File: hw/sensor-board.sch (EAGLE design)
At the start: 17 parts, among them U1 LT1762EMS8-3.3PBF, U2 ULN2003LVPWR, U3 ULN2003LVPWR, U4 PCA9685PW, U5 AT42QT1110-AU, X1 MOLEX-501331-1007, X2 MOLEX-501953-0407, X3 MOLEX-501953-0407, X4 MOLEX-501953-0407

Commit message: Connect capsense controller/buttons/B2B connector.
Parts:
- added C10, C11, C12, C5, C6, C7, C8, C9: 0.015uF 16V, rcl:C-EUC0402K
- added R1, R2, R3, R4, R5, R6, R7, R8: 4.7k, myrcl:R-EU_NKR0402
- added TP1, TP2, TP3, TP4: PTR1TP06R, testpad:PTR1TP06R
- C2, C3, C4: device rcl:C-EUC0603K -> rcl:C-EUC0402K
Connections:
- net N$6 renamed VDD_3_3
- new net N$10: C8.1, U5.SNS3
- new net N$11: C9.1, U5.SNS4
- new net N$12: C10.1, U5.SNS5
- new net N$13: C11.1, U5.SNS6
- new net N$14: C12.1, U5.SNS7/DETECT1
- new net N$15: C5.2, R1.1, U5.SNS0K
- new net N$16: C6.2, R2.1, U5.SNS1K
- new net N$17: C7.2, R3.1, U5.SNS2K
- new net N$18: C8.2, R4.1, U5.SNS3K
- new net N$19: C9.2, R5.1, U5.SNS4K
- new net N$20: C10.2, R6.1, U5.SNS5K
- new net N$21: C11.2, R7.1, U5.SNS6K
- new net N$22: C12.2, R8.1, U5.SNS7K/DETECT0
- new net N$23: R5.2, X4.1
- new net N$24: R6.2, X4.2
- new net N$25: R7.2, X4.3
- new net N$26: R8.2, X4.4
- new net N$27: R4.2, TP4.TP, X3.4
- new net N$28: R3.2, TP3.TP, X3.3
- new net N$29: R2.2, TP2.TP, X3.2
- new net N$30: R1.2, TP1.TP, X3.1
- new net N$6: C5.1, U5.SNS0
- new net N$7: C6.1, U5.SNS1
- new net N$9: C7.1, U5.SNS2
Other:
- note added: "LAYOUT CLOSE TO IC"
- moved on the sheet: C3, D1, D2, D3, D4, U2, U3, U4, X3, X4

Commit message: Partly complete layout.
Pending schematic tasks:
1.  Replace 10 pin sensor board to main board connector with a higher
    pin count variant for unrouted signals on LED controller and
    RST,CHANGE pins on touch controller.
2.  Add pull ups on control and comm lines of touch and led ICs,
    as needed.
3.  Add mecahnism to set I2C address on LED controller.
4.  Identify purpose of and route COM pin on ULN2003LV.

Pending layout tasks:
1.  Route power and ground to top half and bottom right parts of board.
2.  Consider rotating touch IC 90 degrees counter clockwise to better
    match positions of b2b sensor connector and capsense buttons.
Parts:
- removed TP1, TP2, TP3, TP4: PTR1TP06R, testpad:PTR1TP06R
- added C13, C14, C15, C16, C17, C18, C19, C20, C21, C22, C23, C24: 0.01uF 16V, rcl:C-EUC0402K
- added R10, R11, R12, R13, R14, R15, R16, R17, R18, R19, R20, R9: 60R 145mW, myrcl:R-EU_NKR0603
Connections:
- removed net N$27: R4.2, TP4.TP, X3.4
- removed net N$28: R3.2, TP3.TP, X3.3
- removed net N$29: R2.2, TP2.TP, X3.2
- removed net N$30: R1.2, TP1.TP, X3.1
- new net KEY1: R1.2, X3.1
- new net KEY2: R2.2, X3.2
- new net KEY3: R3.2, X3.3
- new net KEY4: R4.2, X3.4
- new net LEDOUT_A1: U2.IN1, U4.LED0
- new net LEDOUT_A2: U2.IN2, U4.LED1
- new net LEDOUT_A3: U2.IN3, U4.LED2
- new net LEDOUT_A4: U2.IN4, U4.LED3
- new net LEDOUT_A5: U2.IN5, U4.LED4
- new net LEDOUT_A6: U2.IN6, U4.LED5
- new net LEDOUT_B1: U3.IN1, U4.LED6
- new net LEDOUT_B2: U3.IN2, U4.LED7
- new net LEDOUT_B3: U3.IN3, U4.LED8
- new net LEDOUT_B4: U3.IN4, U4.LED9
- new net LEDOUT_B5: U3.IN5, U4.LED10
- new net LEDOUT_B6: U3.IN6, U4.LED11
- new net N$31: D4.1-CB, R20.2
- new net N$32: D1.1-CB, R11.2
- new net N$33: D1.2-CG, R10.2
- new net N$34: D3.3-CR, R15.2
- new net N$35: D2.3-CR, R12.2
- new net N$36: D2.2-CG, R13.2
- new net N$37: R15.1, U3.OUT1
- new net N$38: R16.1, U3.OUT2
- new net N$39: D3.1-CB, R17.2
- new net N$40: D3.2-CG, R16.2
- new net N$41: D4.3-CR, R18.2
- new net N$42: D4.2-CG, R19.2
- new net N$55: R17.1, U3.OUT3
- new net N$56: R18.1, U3.OUT4
- new net N$57: R19.1, U3.OUT5
- new net N$58: R20.1, U3.OUT6
- new net N$59: D2.1-CB, R14.2
- new net N$60: D1.3-CR, R9.2
- new net N$61: R9.1, U2.OUT1
- new net N$62: R10.1, U2.OUT2
- new net N$63: R11.1, U2.OUT3
- new net N$64: R12.1, U2.OUT4
- new net N$65: R13.1, U2.OUT5
- new net N$66: R14.1, U2.OUT6
- new net SCL: U4.SCL, X2.4
- new net SDA: U4.SDA, X2.3
- net GND: now also C13.1, C14.1, C15.1, C16.1, C17.1, C18.1, C19.1, C20.1, C21.1, C22.1, C23.1, C24.1, U2.GND, U3.GND, U4.GND, X2.2
- net VDD_5: now also C13.2, C14.2, C15.2, C16.2, C17.2, C18.2, C19.2, C20.2, C21.2, C22.2, C23.2, C24.2, D1.4-AR, D1.5-AG, D1.6-AB, D2.4-AR, D2.5-AG, D2.6-AB, D3.4-AR, D3.5-AG, D3.6-AB, D4.4-AR, D4.5-AG, D4.6-AB, U4.VDD, X1.1, X2.1
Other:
- moved on the sheet: C1, C10, C11, C12, C2, C3, C4, C5, C6, C7, C8, C9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

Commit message: Compact the layout of LED driving circuitry.
Additional space has been created for a larger sensor to main board
connector.
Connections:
- net GND: now also U4.A2, U4.A3, U4.A4, U4.A5, U4.EXTCLK
- net VDD_5: now also U2.COM, U3.COM
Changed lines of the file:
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@@
 <grid distance="0.1" unitdist="inch" unit="inch" style="lines" multiple="1" display="no" altdistance="0.01" altunitdist="inch" altunit="inch"/>
 <layers>
-<layer number="1" name="Top" color="4" fill="1" visible="yes" active="no"/>
-<layer number="16" name="Bottom" color="1" fill="1" visible="yes" active="no"/>
-<layer number="17" name="Pads" color="2" fill="1" visible="yes" active="no"/>
-<layer number="18" name="Vias" color="2" fill="1" visible="yes" active="no"/>
-<layer number="19" name="Unrouted" color="6" fill="1" visible="yes" active="no"/>
-<layer number="20" name="Dimension" color="15" fill="1" visible="yes" active="no"/>
-<layer number="21" name="tPlace" color="7" fill="1" visible="yes" active="no"/>
-<layer number="22" name="bPlace" color="7" fill="1" visible="yes" active="no"/>
-<layer number="23" name="tOrigins" color="15" fill="1" visible="yes" active="no"/>
-<layer number="24" name="bOrigins" color="15" fill="1" visible="yes" active="no"/>
-<layer number="25" name="tNames" color="7" fill="1" visible="yes" active="no"/>
-<layer number="26" name="bNames" color="7" fill="1" visible="yes" active="no"/>
-<layer number="27" name="tValues" color="7" fill="1" visible="yes" active="no"/>
-<layer number="28" name="bValues" color="7" fill="1" visible="yes" active="no"/>
+<layer number="1" name="Top" color="4" fill="1" visible="no" active="no"/>
+<layer number="16" name="Bottom" color="1" fill="1" visible="no" active="no"/>
+<layer number="17" name="Pads" color="2" fill="1" visible="no" active="no"/>
+<layer number="18" name="Vias" color="2" fill="1" visible="no" active="no"/>
+<layer number="19" name="Unrouted" color="6" fill="1" visible="no" active="no"/>
+<layer number="20" name="Dimension" color="15" fill="1" visible="no" active="no"/>
+<layer number="21" name="tPlace" color="7" fill="1" visible="no" active="no"/>
+<layer number="22" name="bPlace" color="7" fill="1" visible="no" active="no"/>
+<layer number="23" name="tOrigins" color="15" fill="1" visible="no" active="no"/>
+<layer number="24" name="bOrigins" color="15" fill="1" visible="no" active="no"/>
+<layer number="25" name="tNames" color="7" fill="1" visible="no" active="no"/>
+<layer number="26" name="bNames" color="7" fill="1" visible="no" active="no"/>
+<layer number="27" name="tValues" color="7" fill="1" visible="no" active="no"/>
+<layer number="28" name="bValues" color="7" fill="1" visible="no" active="no"/>
 <layer number="29" name="tStop" color="7" fill="3" visible="no" active="no"/>
 <layer number="30" name="bStop" color="7" fill="6" visible="no" active="no"/>
@@
 <layer number="35" name="tGlue" color="7" fill="4" visible="no" active="no"/>
 <layer number="36" name="bGlue" color="7" fill="5" visible="no" active="no"/>
-<layer number="37" name="tTest" color="7" fill="1" visible="yes" active="no"/>
-<layer number="38" name="bTest" color="7" fill="1" visible="yes" active="no"/>
+<layer number="37" name="tTest" color="7" fill="1" visible="no" active="no"/>
+<layer number="38" name="bTest" color="7" fill="1" visible="no" active="no"/>
 <layer number="39" name="tKeepout" color="4" fill="11" visible="no" active="no"/>
 <layer number="40" name="bKeepout" color="1" fill="11" visible="no" active="no"/>
@@
 <layer number="44" name="Drills" color="7" fill="1" visible="no" active="no"/>
 <layer number="45" name="Holes" color="7" fill="1" visible="no" active="no"/>
-<layer number="46" name="Milling" color="3" fill="1" visible="yes" active="no"/>
-<layer number="47" name="Measures" color="7" fill="1" visible="yes" active="no"/>
-<layer number="48" name="Document" color="7" fill="1" visible="yes" active="no"/>
-<layer number="49" name="Reference" color="7" fill="1" visible="yes" active="no"/>
-<layer number="51" name="tDocu" color="7" fill="1" visible="yes" active="no"/>
-<layer number="52" name="bDocu" color="7" fill="1" visible="yes" active="no"/>
+<layer number="46" name="Milling" color="3" fill="1" visible="no" active="no"/>
+<layer number="47" name="Measures" color="7" fill="1" visible="no" active="no"/>
+<layer number="48" name="Document" color="7" fill="1" visible="no" active="no"/>
+<layer number="49" name="Reference" color="7" fill="1" visible="no" active="no"/>
+<layer number="51" name="tDocu" color="7" fill="1" visible="no" active="no"/>
+<layer number="52" name="bDocu" color="7" fill="1" visible="no" active="no"/>
 <layer number="91" name="Nets" color="2" fill="1" visible="yes" active="yes"/>
 <layer number="92" name="Busses" color="1" fill="1" visible="yes" active="yes"/>
@@
 <wire x1="353.06" y1="-25.4" x2="500.38" y2="-25.4" width="0.1524" layer="91"/>
 <wire x1="500.38" y1="86.36" x2="500.38" y2="-25.4" width="0.1524" layer="91"/>
+<pinref part="U3" gate="A" pin="COM"/>
+<wire x1="287.02" y1="-38.1" x2="518.16" y2="-38.1" width="0.1524" layer="91"/>
+<wire x1="518.16" y1="-38.1" x2="518.16" y2="17.78" width="0.1524" layer="91"/>
+<wire x1="518.16" y1="17.78" x2="518.16" y2="86.36" width="0.1524" layer="91"/>
+<wire x1="518.16" y1="86.36" x2="500.38" y2="86.36" width="0.1524" layer="91"/>
+<pinref part="U2" gate="A" pin="COM"/>
+<wire x1="287.02" y1="17.78" x2="518.16" y2="17.78" width="0.1524" layer="91"/>
+<junction x="518.16" y="17.78"/>
 </segment>
 </net>
@@
 <wire x1="93.98" y1="218.44" x2="93.98" y2="99.06" width="0.1524" layer="91"/>
 <junction x="93.98" y="99.06"/>
+<pinref part="U4" gate="G$1" pin="EXTCLK"/>
+<wire x1="127" y1="10.16" x2="106.68" y2="10.16" width="0.1524" layer="91"/>
+<wire x1="106.68" y1="10.16" x2="106.68" y2="-38.1" width="0.1524" layer="91"/>
+<wire x1="106.68" y1="-38.1" x2="121.92" y2="-38.1" width="0.1524" layer="91"/>
+<pinref part="U4" gate="G$1" pin="A5"/>
+<wire x1="121.92" y1="-38.1" x2="147.32" y2="-38.1" width="0.1524" layer="91"/>
+<wire x1="127" y1="-7.62" x2="121.92" y2="-7.62" width="0.1524" layer="91"/>
+<wire x1="121.92" y1="-7.62" x2="121.92" y2="-38.1" width="0.1524" layer="91"/>
+<pinref part="U4" gate="G$1" pin="A2"/>
+<wire x1="127" y1="0" x2="121.92" y2="0" width="0.1524" layer="91"/>
+<wire x1="121.92" y1="0" x2="121.92" y2="-2.54" width="0.1524" layer="91"/>
+<pinref part="U4" gate="G$1" pin="A3"/>
+<wire x1="121.92" y1="-2.54" x2="121.92" y2="-5.08" width="0.1524" layer="91"/>
+<wire x1="121.92" y1="-5.08" x2="121.92" y2="-7.62" width="0.1524" layer="91"/>
+<wire x1="127" y1="-2.54" x2="121.92" y2="-2.54" width="0.1524" layer="91"/>
+<pinref part="U4" gate="G$1" pin="A4"/>
+<wire x1="127" y1="-5.08" x2="121.92" y2="-5.08" width="0.1524" layer="91"/>
 </segment>
 </net>

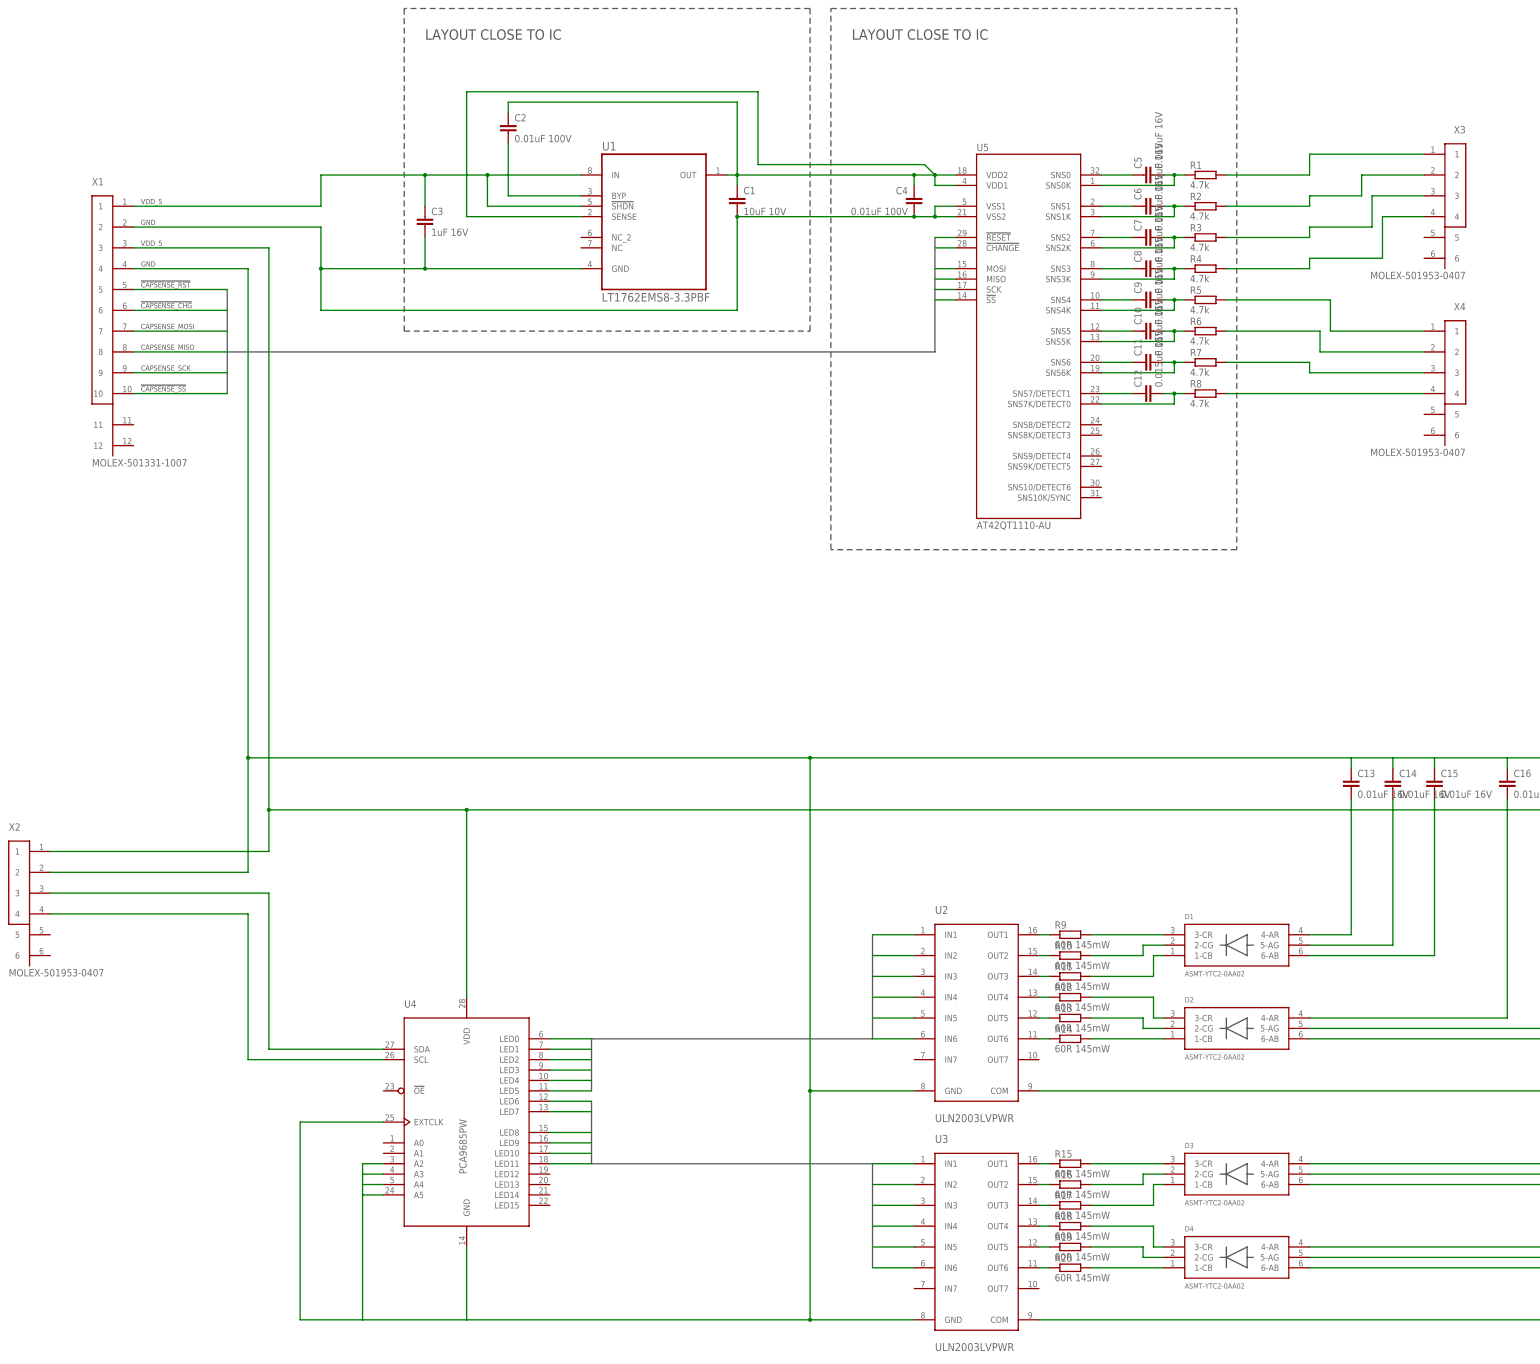
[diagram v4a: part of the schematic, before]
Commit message: Change capsense IC to QT1070. Routing finished.
Schematic and routing need to be checked against LED and CAPSENSE IC
datasheets wrt operational requirements.
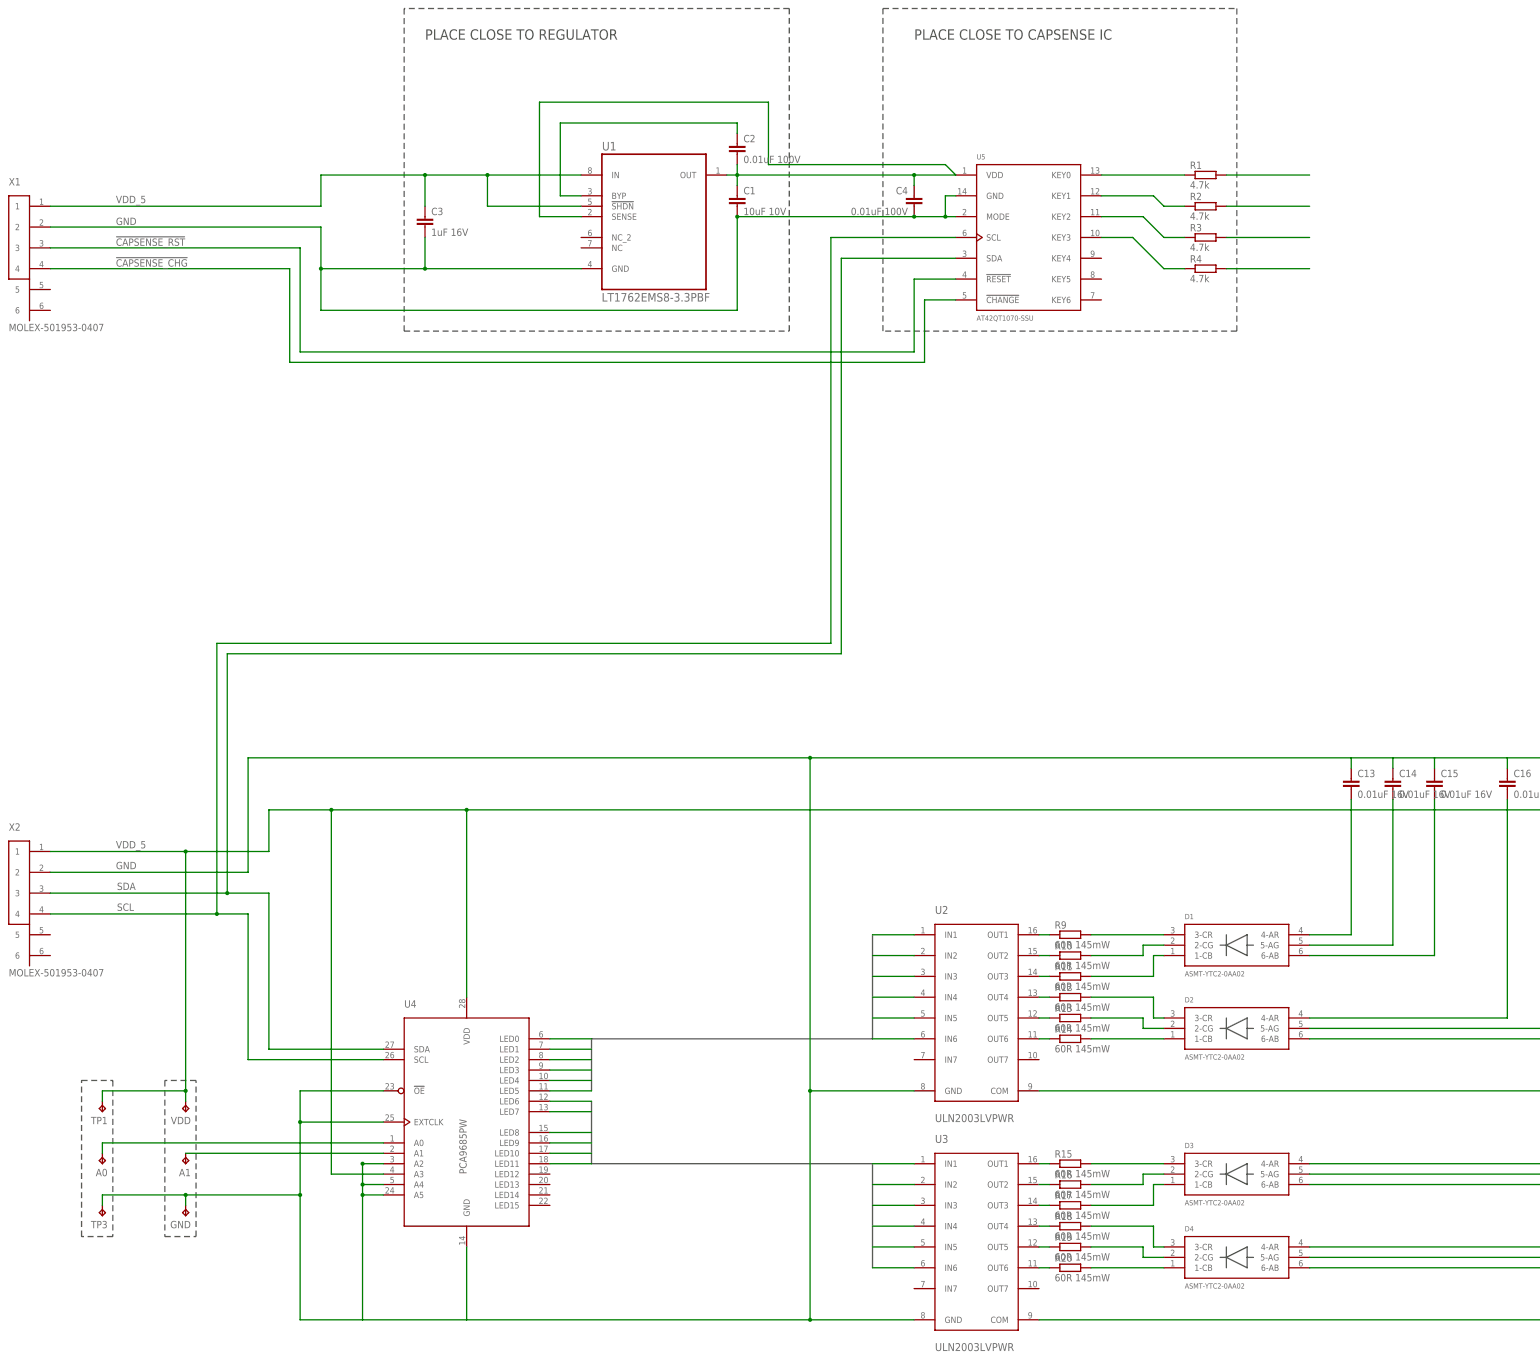
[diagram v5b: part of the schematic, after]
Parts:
- removed C10, C11, C12, C5, C6, C7, C8, C9: 0.015uF 16V, rcl:C-EUC0402K
- removed R5, R6, R7, R8: 4.7k, myrcl:R-EU_NKR0402
- removed X3, X4: MOLEX-501953-0407, connector:MOLEX-501953-0407
- added A0, A1, GND, TP1, TP3, VDD: TPB1,27, testpad:TPB1,27
- U5: value AT42QT1110-AU -> AT42QT1070-SSU; device touch_ctl:AT42QT1110-AU -> touch_ctl:AT42QT1070-SSU
- X1: value MOLEX-501331-1007 -> MOLEX-501953-0407; device connector:MOLEX-501331-1007 -> connector:MOLEX-501953-0407
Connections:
- removed net CAPSENSE1: U5.!RESET!, X1.5
- removed net CAPSENSE2: U5.!CHANGE!, X1.6
- removed net CAPSENSE3: U5.MOSI, X1.7
- removed net CAPSENSE4: U5.MISO, X1.8
- removed net CAPSENSE5: U5.SCK, X1.9
- removed net CAPSENSE6: U5.!SS!, X1.10
- removed net N$10: C8.1, U5.SNS3
- removed net N$11: C9.1, U5.SNS4
- removed net N$12: C10.1, U5.SNS5
- removed net N$13: C11.1, U5.SNS6
- removed net N$14: C12.1, U5.SNS7/DETECT1
- removed net N$19: C9.2, R5.1, U5.SNS4K
- removed net N$20: C10.2, R6.1, U5.SNS5K
- removed net N$21: C11.2, R7.1, U5.SNS6K
- removed net N$22: C12.2, R8.1, U5.SNS7K/DETECT0
- removed net N$23: R5.2, X4.1
- removed net N$24: R6.2, X4.2
- removed net N$25: R7.2, X4.3
- removed net N$26: R8.2, X4.4
- removed net N$9: C7.1, U5.SNS2
- new net !CAPSENSE_CHG!: U5.!CHANGE!, X1.4
- new net !CAPSENSE_RST!: U5.!RESET!, X1.3
- net GND: now also GND.TP, TP3.TP, U4.!OE!, U5.GND, U5.MODE; no longer U4.A3, U5.VSS1, U5.VSS2, X1.4
- net KEY1: no longer X3.1
- net KEY2: no longer X3.2
- net KEY3: no longer X3.3
- net KEY4: no longer X3.4
- net N$15: now also U5.KEY0; no longer C5.2, U5.SNS0K
- net N$16: now also U5.KEY1; no longer C6.2, U5.SNS1K
- net N$17: now also U5.KEY2; no longer C7.2, U5.SNS2K
- net N$18: now also U5.KEY3; no longer C8.2, U5.SNS3K
- net N$6: now also A0.TP, U4.A0; no longer C5.1, U5.SNS0
- net N$7: now also A1.TP, U4.A1; no longer C6.1, U5.SNS1
- net N$8: now also C2.1; no longer C2.2
- net SCL: now also U5.SCL
- net SDA: now also U5.SDA
- net VDD_3_3: now also C2.2, U5.VDD; no longer C2.1, U5.VDD1, U5.VDD2
- net VDD_5: now also TP1.TP, U4.A3, VDD.TP; no longer X1.3
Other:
- note added: "PLACE CLOSE TO CAPSENSE IC"
- note added: "PLACE CLOSE TO REGULATOR"
- note removed: "!CAPSENSE_CHG!"
- note removed: "!CAPSENSE_RST!"
- note removed: "!CAPSENSE_SS!"
- note removed: "CAPSENSE_MISO"
- note removed: "CAPSENSE_MOSI"
- note removed: "CAPSENSE_SCK"
- note removed: "GND"
- note removed: "LAYOUT CLOSE TO IC"
- note removed: "VDD_5"
- moved on the sheet: C2
